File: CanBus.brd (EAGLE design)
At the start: 80 x 100 mm, 59 parts, among them IC1 MCP2515-I/SO, IC2 MEGA8-AI, IC3 MCP2515-I/SO, Q1 16MHz, Q2 16MHz, Q3 16MHz, U1 MCP2562-E/SN, U2 MCP2562-E/SN, X1 MAC64L

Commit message: Layouts angepasst
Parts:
- added J2, J3: (no value), mebp_8-8g:MEBP_8-8G
- added JP1, JP3: (no value), jumper:JP1
- added R10, R9: 4k7, rcl:R1206
- R1, R4: value 4k7 -> 120R
- moved R1 49.6 mm to (71.1, 15.9)
- moved R2 38.2 mm to (71.1, 34.9), turned to 180 degrees
- moved R3 34.6 mm to (71.1, 54.0)
- moved JP2 22.5 mm to (71.1, 37.5), turned to 270 degrees
- moved R4 14.0 mm to (38.7, 43.8), turned to 180 degrees
- moved J1 12.5 mm to (85.1, 13.3)
- moved LED1 11.7 mm to (86.4, 63.5)
- moved LED2 11.7 mm to (86.4, 68.6)
- moved LED3 11.7 mm to (86.4, 73.7)
- moved R6 11.4 mm to (71.1, 67.3)
- moved R7 11.4 mm to (71.1, 69.8)
- moved R8 11.4 mm to (71.1, 72.4)
- moved AT-RESET 11.4 mm to (59.7, 83.2)
- moved AT-PROG 11.4 mm to (82.5, 85.1)
- moved C11 10.8 mm to (67.6, 81.0)
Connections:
- new net CANH_1: J1.7, J2.2, R1.1
- new net CANH_3: J3.7, R3.1
- new net CANL_1: J1.8, J2.1, JP1.2
- new net CANL_3: J3.8, JP3.2
- new net N$12: JP3.1, R3.2
- new net N$8: JP1.1, R1.2
- net +24V: now also J2.4, J2.5, J3.4, J3.5
- net +3,3V: now also R10.2, R9.2; no longer R1.2, R4.2
- net CANH: now also R4.1; no longer R2.1
- net CANH_2: now also J2.7, J3.2, R2.1; no longer J1.7, R3.1
- net CANL: now also R4.2; no longer R2.2
- net CANL_2: now also J2.8, J3.1; no longer J1.8
- net GND: now also J2.3, J2.6, J2.G1, J2.G2, J3.3, J3.6, J3.G1, J3.G2
- net N$2: now also R9.1; no longer R1.1
- net N$3: now also R2.2; no longer R3.2
- net N$5: now also R10.1; no longer R4.1
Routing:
- net +24V: track 159.0 -> 204.6 mm
- net CANH_1: track 0.00 -> 20.2 mm
- net CANL_1: track 0.00 -> 16.4 mm
- net CANH_2: track 6.83 -> 20.2 mm
- net PROG_TX: track 34.9 -> 46.4 mm
- net PROG_RX: track 35.8 -> 47.2 mm
- net LED3: track 19.7 -> 31.1 mm
- net LED2: track 20.4 -> 31.8 mm
- net LED1: track 22.6 -> 34.0 mm
- net CANL: track 68.0 -> 79.3 mm
- net CANH: track 64.2 -> 75.5 mm
- net !AT_RESET: track 43.5 -> 54.3 mm
- net CANH_3: track 0.00 -> 6.46 mm
- net CANL_2: track 11.3 -> 16.4 mm
- net CANL_3: track 0.00 -> 4.07 mm
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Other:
- board size 80 x 100 mm -> 91.4 x 100 mm
- board text added: "End-Terminierung mit T1, T2 oder T3, abhängig vom letzten verwendeten Port"
- board text added: "T1"
- board text added: "T2"
- board text added: "T3"
- board text removed: "CAN-2 Terminierung"

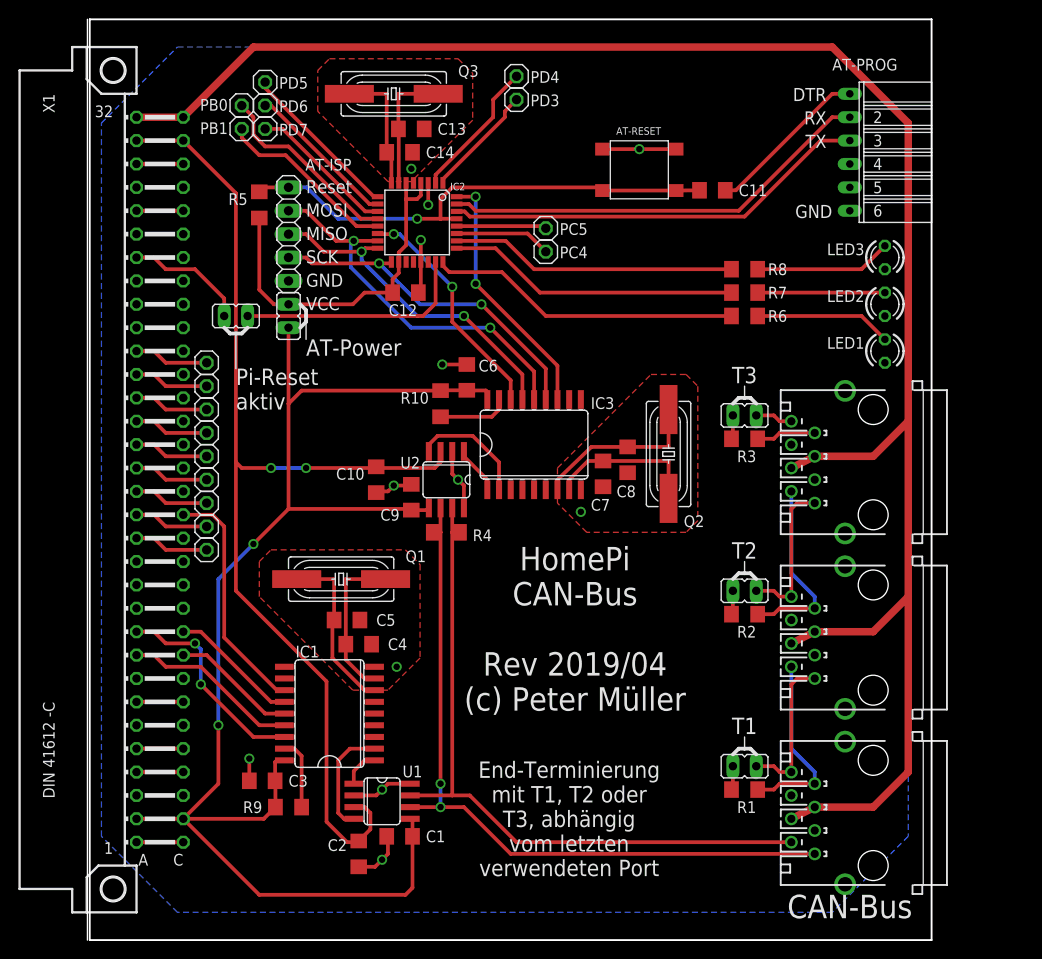
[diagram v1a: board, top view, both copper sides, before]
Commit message: Layouts angepasst, Backplane vergrößert
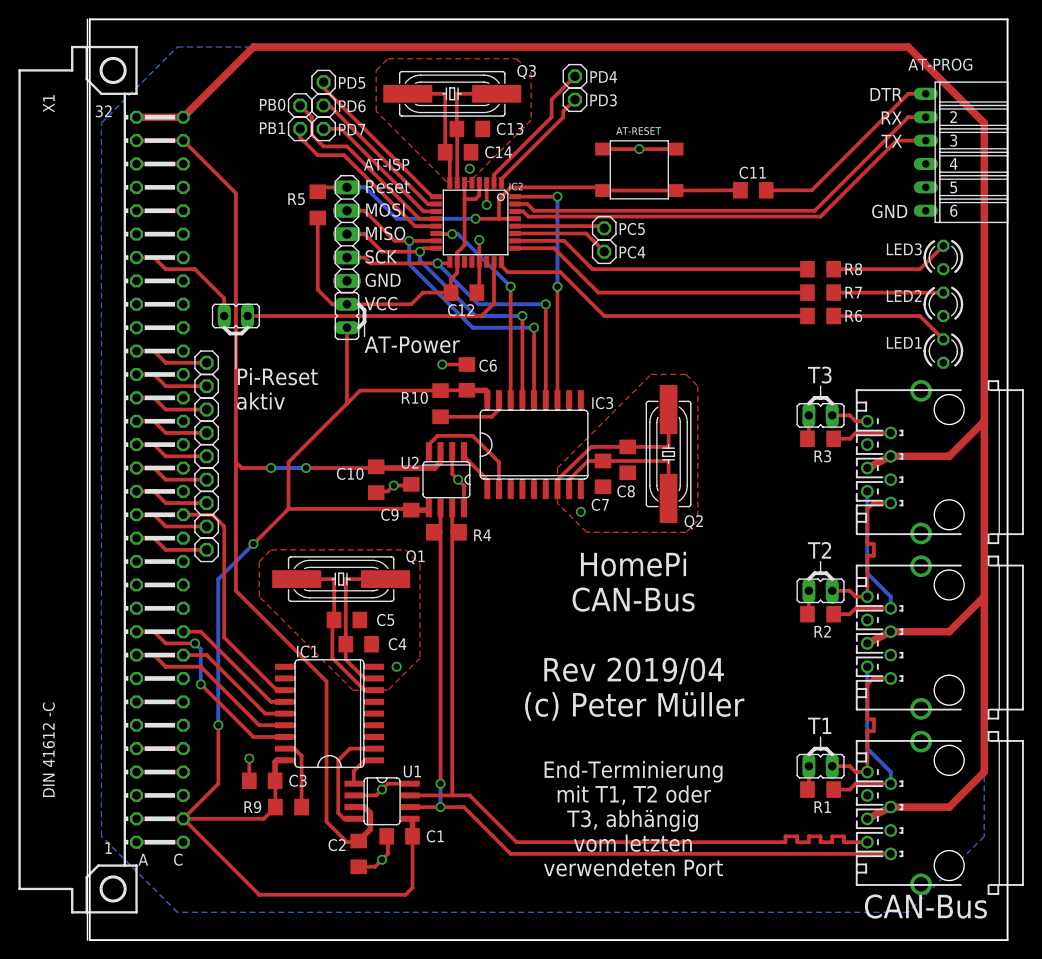
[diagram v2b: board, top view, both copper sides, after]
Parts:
- moved AT-PROG 8.26 mm to (90.8, 85.1)
- moved J1 8.25 mm to (93.3, 13.3)
- moved J2 8.25 mm to (93.3, 32.4)
- moved J3 8.25 mm to (93.3, 51.4)
- moved JP1 8.25 mm to (79.4, 18.4)
- moved JP2 8.25 mm to (79.4, 37.5)
- moved JP3 8.25 mm to (79.4, 56.5)
- moved R1 8.25 mm to (79.4, 15.9)
- moved R2 8.25 mm to (79.4, 34.9)
- moved R3 8.25 mm to (79.4, 54.0)
- moved R6 8.25 mm to (79.4, 67.3)
- moved R7 8.25 mm to (79.4, 69.8)
- moved R8 8.25 mm to (79.4, 72.4)
- moved AT-ISP 6.35 mm to (27.9, 76.2)
- moved AT-PWR 6.35 mm to (27.9, 67.3)
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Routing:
- net CANH: track 75.5 -> 87.5 mm
- net CANL: track 79.3 -> 87.5 mm
- net +24V: track 204.6 -> 212.9 mm
- net N$9: track 25.5 -> 31.8 mm
- net AT_SPI_MOSI: track 41.7 -> 37.8 mm
- net PROG_DTR: track 17.9 -> 21.7 mm
- net +3,3V: track 154.4 -> 150.7 mm
- net AT_SPI_CS: track 25.4 -> 22.7 mm
- net AT_SPI_MISO: track 36.9 -> 34.3 mm
- net AT_SPI_SCK: track 37.7 -> 35.4 mm
- net !AT_RESET: track 54.3 -> 52.4 mm
- net PROG_TX: track 46.4 -> 48.3 mm
- net LED3: track 31.1 -> 33.0 mm
- net LED2: track 31.8 -> 33.7 mm
- net LED1: track 34.0 -> 35.9 mm
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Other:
- board size 91.4 x 100 mm -> 99.7 x 100 mm

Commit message: Layouts angepasst
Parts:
- added U$1: (no value), cryCode-Logo:30MM
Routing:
- net +3,3V: track 150.7 -> 160.5 mm
- net +24V: track 212.9 -> 213.6 mm
- net GND: track 44.5 -> 43.9 mm
- added copper zone on layer 1, net TOP
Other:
- board text added: "BOT"
- board text added: "HomePi CAN-Bus Rev 2019/05 (c) Peter Müller"
- board text added: "TOP"
- board text removed: "HomePi CAN-Bus Rev 2019/04 (c) Peter Müller"

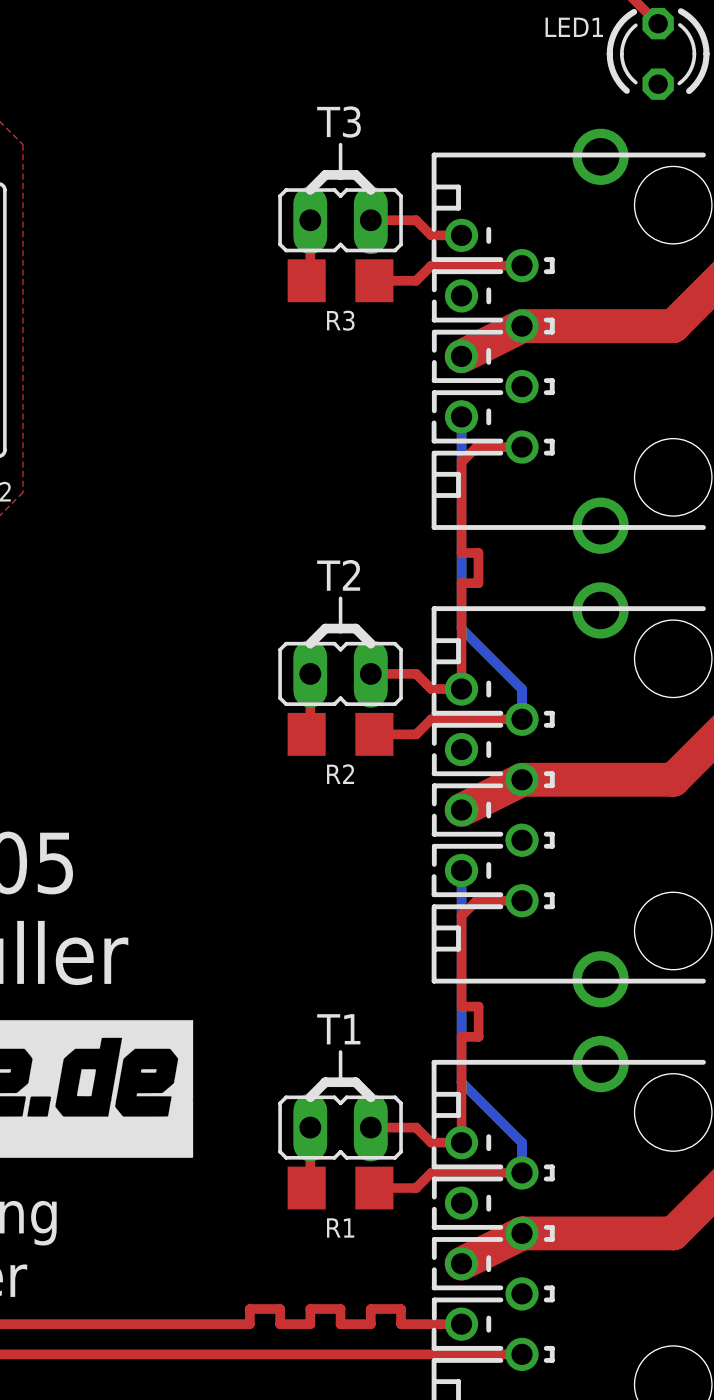
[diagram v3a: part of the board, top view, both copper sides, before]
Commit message: Schaltpläne aufgehübscht zur Veröffentlichung
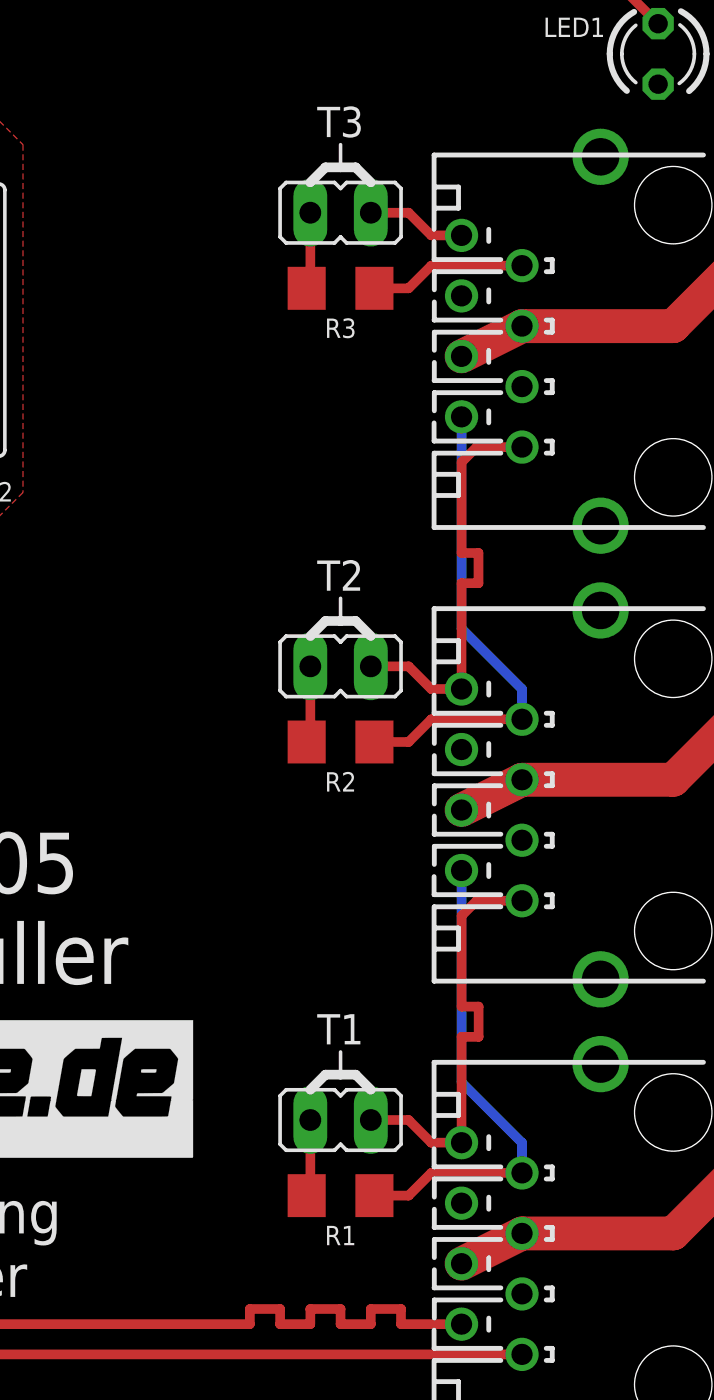
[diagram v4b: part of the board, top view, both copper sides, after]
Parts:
- moved JP1 0.32 mm to (79.4, 18.7)
- moved JP3 0.32 mm to (79.4, 56.8)
- moved R3 0.32 mm to (79.4, 53.7)
- moved R1 0.32 mm to (79.4, 15.6)
- moved JP2 0.32 mm to (79.4, 37.8)
- moved R2 0.32 mm to (79.4, 34.6)
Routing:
- net N$12: track 2.60 -> 3.20 mm
- net N$8: track 2.69 -> 3.21 mm
- net N$3: track 2.69 -> 3.21 mm
